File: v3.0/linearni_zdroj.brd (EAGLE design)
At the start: 39.4 x 77.1 mm, 37 parts, among them IC1 LM358N, IC2 LM358N, Q1 IRFZ34NAV, Q2 TIP120

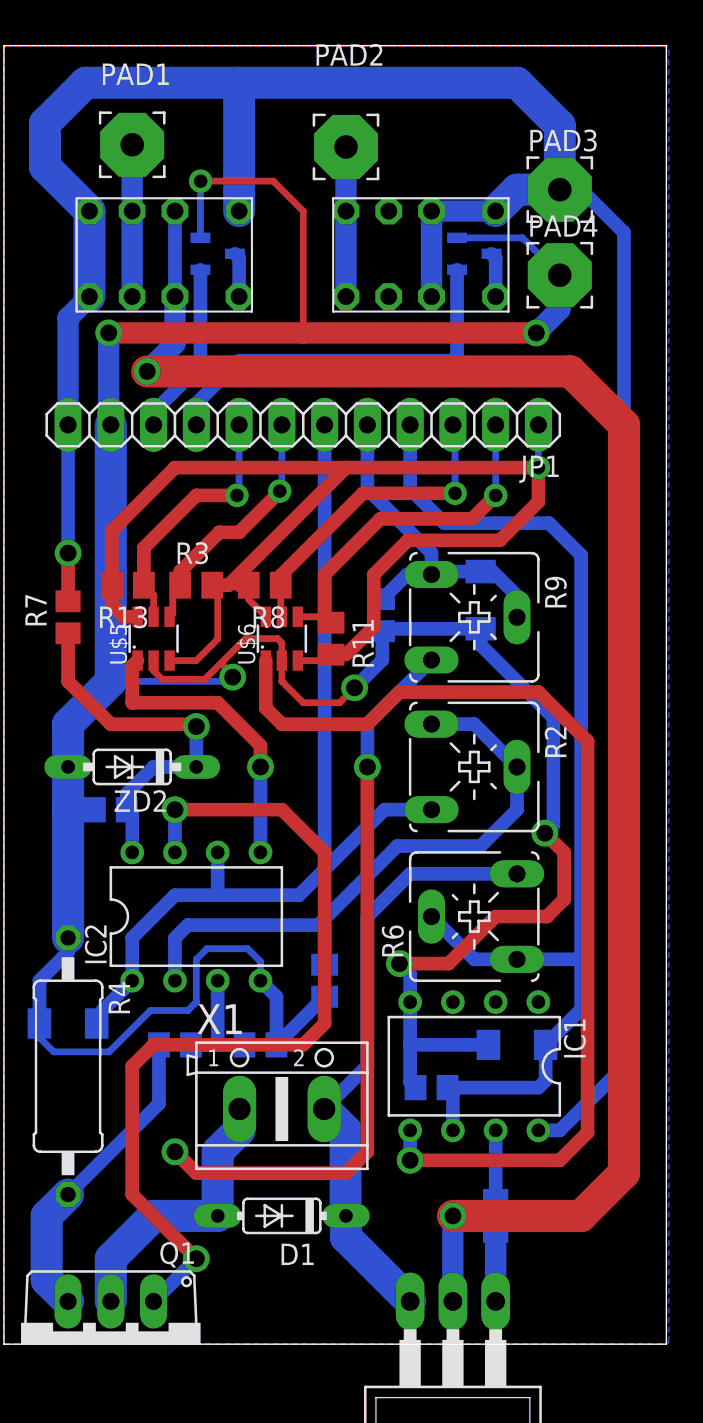
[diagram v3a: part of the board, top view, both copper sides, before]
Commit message: přidání 3D modelu úpravy dokumentace
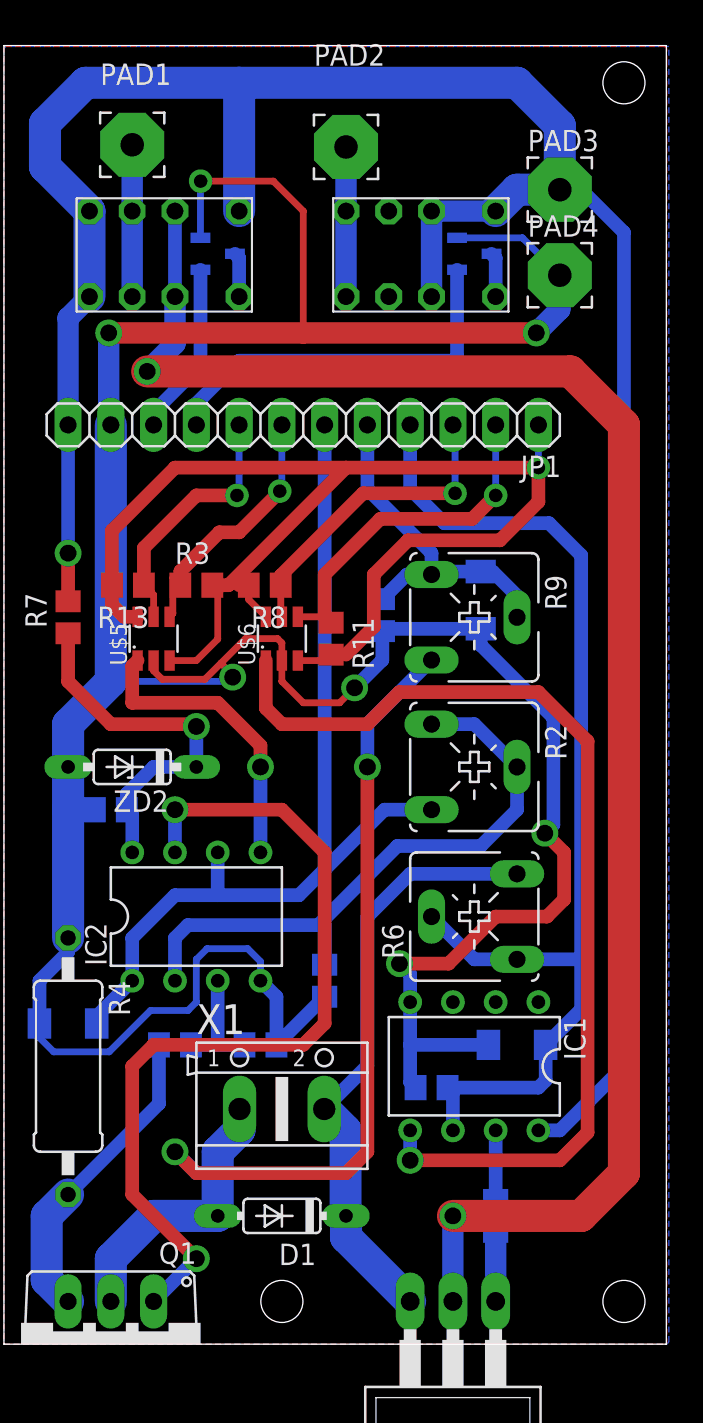
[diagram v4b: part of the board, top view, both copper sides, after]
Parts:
- R1, R11, R13, R3, R8: device rcl_my:M0805 -> rcl:R0805

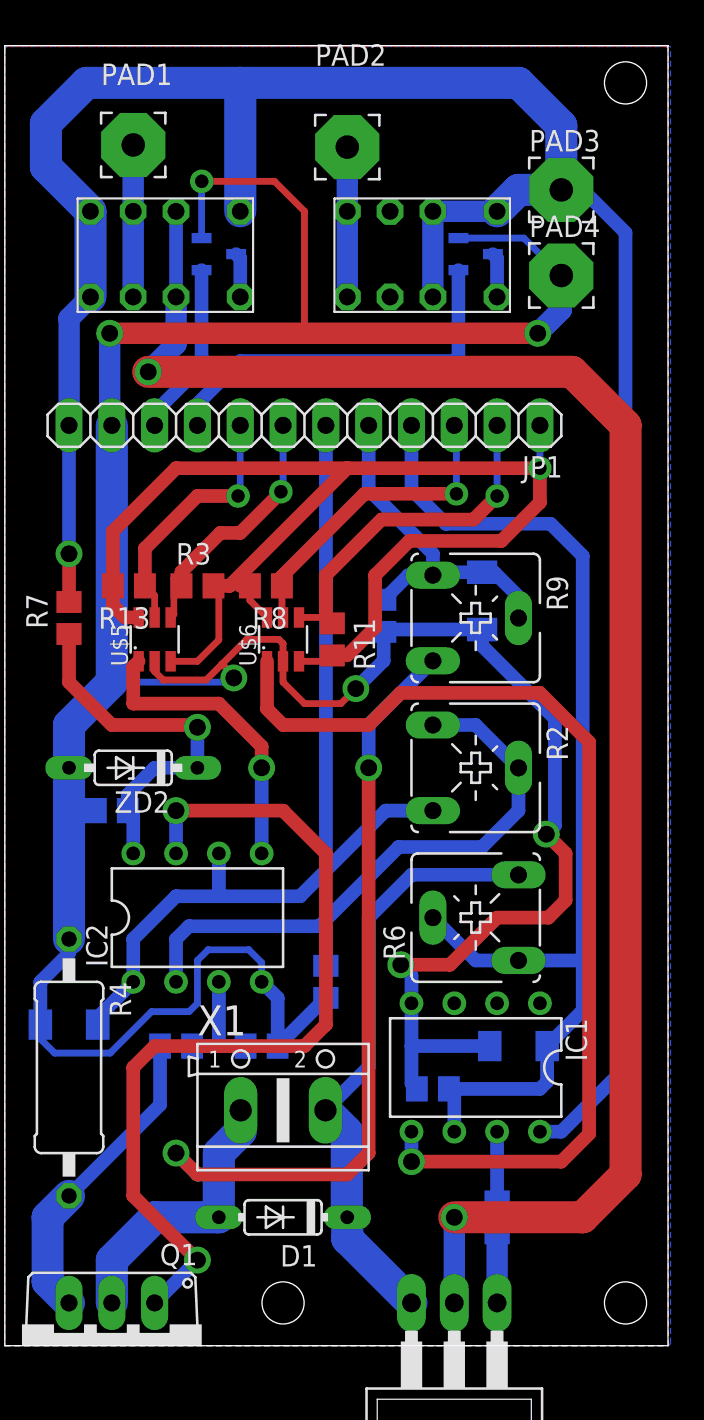
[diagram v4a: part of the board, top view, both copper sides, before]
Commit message: upratování schémy, dokumentace lineárního regulátoru napětí
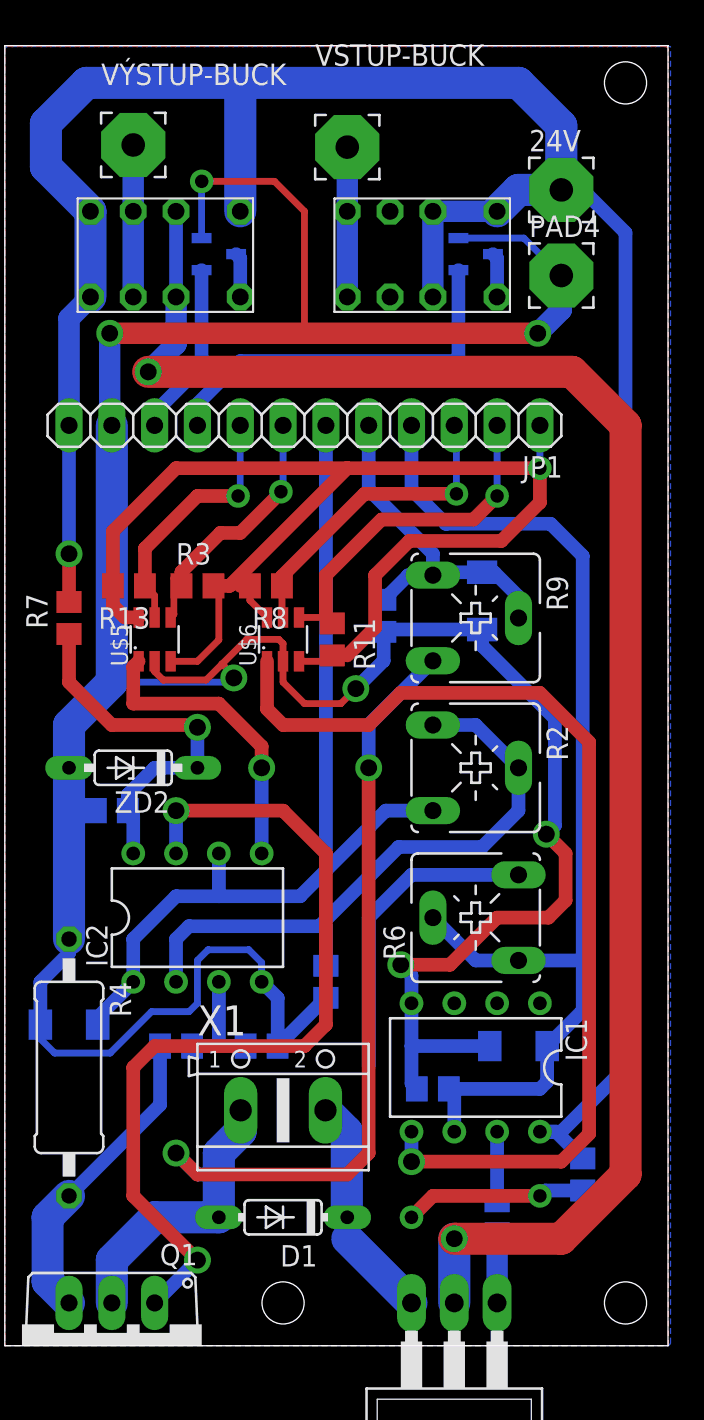
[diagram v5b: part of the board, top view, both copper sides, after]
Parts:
- added C2: 10n, rcl:C0805
- R11, R8: value (none) -> 5K
- R12: value (none) -> 360R
- renumbered PAD1 to VÝSTUP-BUCK, PAD2 to VSTUP-BUCK, PAD3 to 24V
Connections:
- net N$13 renamed +
- net N$8 renamed NAPAJENI-REG
- net +24V: now also C2.1
- net GND: now also C2.2
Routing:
- net GND: track 206.7 -> 217.5 mm, vias 7 -> 9
- net +: track 36.0 -> 31.1 mm
- net +24V: track 148.3 -> 151.5 mm
- net NAPAJENI-REG: track 100.6 -> 99.8 mm

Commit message: zase sem se jednou ve škole něco naučil
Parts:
- removed C1: (no value), rcl:C0805
- moved R14 13.1 mm to (16.5, 6.35), flipped to the top, turned to 180 degrees
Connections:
- removed net N$1: Q1.S, R14.2, R4.2
- net GND: now also R14.1; no longer C1.2
- net N$2: now also R14.2
- net N$20: now also Q1.S, R4.2; no longer C1.1, R14.1
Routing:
- net N$1: track 18.5 -> 0.00 mm
- net N$20: track 6.99 -> 23.8 mm
- net N$2: track 51.7 -> 56.4 mm
- net GND: track 217.5 -> 219.1 mm, vias 9 -> 11
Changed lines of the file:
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@@
 <attribute name="VALUE" x="8.636" y="47.625" size="1.27" layer="27" rot="R180"/>
-</element>
-<element name="R14" library="rcl" library_urn="urn:adsk.eagle:library:334" package="R0805" package3d_urn="urn:adsk.eagle:package:23553/2" value="" x="10.16" y="17.78" smashed="yes" rot="MR0">
-<attribute name="NAME" x="10.795" y="19.05" size="1.27" layer="26" rot="MR0"/>
-<attribute name="POPULARITY" value="86" x="10.16" y="17.78" size="1.778" layer="28" rot="MR0" display="off"/>
-<attribute name="SPICEPREFIX" value="R" x="10.16" y="17.78" size="1.778" layer="28" rot="MR0" display="off"/>
-<attribute name="VALUE" x="10.795" y="15.24" size="1.27" layer="28" rot="MR0"/>
-</element>
-<element name="C1" library="rcl" library_urn="urn:adsk.eagle:library:334" package="C0805" package3d_urn="urn:adsk.eagle:package:23617/2" value="" x="15.24" y="17.78" smashed="yes" rot="MR180">
-<attribute name="NAME" x="13.97" y="16.51" size="1.27" layer="26" rot="MR180"/>
-<attribute name="POPULARITY" value="88" x="15.24" y="17.78" size="1.778" layer="28" rot="MR180" display="off"/>
-<attribute name="SPICEPREFIX" value="C" x="15.24" y="17.78" size="1.778" layer="28" rot="MR180" display="off"/>
-<attribute name="VALUE" x="13.97" y="20.32" size="1.27" layer="28" rot="MR180"/>
 </element>
 <element name="Q1" library="devices" package="TO220AV" override_package3d_urn="urn:adsk.eagle:package:33936961/2" override_package_urn="urn:adsk.eagle:footprint:33936962/1" value="IRFZ34NAV" x="6.35" y="0" smashed="yes" rot="R180">
@@
 <attribute name="VALUE" x="36.83" y="11.43" size="1.27" layer="28" rot="MR270"/>
 </element>
+<element name="R14" library="rcl" library_urn="urn:adsk.eagle:library:334" package="R0805" package3d_urn="urn:adsk.eagle:package:23553/2" value="" x="16.51" y="6.35" smashed="yes" rot="R180">
+<attribute name="NAME" x="17.145" y="5.08" size="1.27" layer="25" rot="R180"/>
+<attribute name="POPULARITY" value="86" x="16.51" y="6.35" size="1.778" layer="27" rot="R180" display="off"/>
+<attribute name="SPICEPREFIX" value="R" x="16.51" y="6.35" size="1.778" layer="27" rot="R180" display="off"/>
+<attribute name="VALUE" x="17.145" y="8.89" size="1.27" layer="27" rot="R180"/>
+</element>
 </elements>
 <signals>
-<signal name="N$1">
-<contactref element="R4" pad="2"/>
-<contactref element="R14" pad="2"/>
-<contactref element="Q1" pad="S"/>
-<wire x1="3.81" y1="2.54" x2="2.54" y2="3.81" width="1.905" layer="16"/>
-<wire x1="2.54" y1="7.62" x2="3.81" y2="8.89" width="1.905" layer="16"/>
-<wire x1="2.54" y1="3.81" x2="2.54" y2="7.62" width="1.905" layer="16"/>
-<wire x1="9.21" y1="17.78" x2="9.21" y2="14.29" width="0.8128" layer="16"/>
-<wire x1="9.21" y1="14.29" x2="3.81" y2="8.89" width="0.8128" layer="16"/>
-</signal>
 <signal name="N$3">
 <contactref element="IC2" pad="2"/>
@@
 <contactref element="ZD3" pad="A"/>
 <contactref element="PAD4" pad="1"/>
-<contactref element="C1" pad="2"/>
 <wire x1="11.6753" y1="65.72" x2="11.6753" y2="69.0793" width="0.4064" layer="16"/>
 <wire x1="11.6753" y1="69.0793" x2="11.684" y2="69.088" width="0.4064" layer="16"/>
@@
 <wire x1="3.81" y1="23.29" x2="2.11" y2="21.59" width="0.8128" layer="16"/>
 <wire x1="3.81" y1="23.29" x2="3.81" y2="24.13" width="0.8128" layer="16"/>
-<wire x1="16.19" y1="17.78" x2="16.19" y2="20.64" width="0.8128" layer="16"/>
-<wire x1="16.19" y1="20.64" x2="15.24" y2="21.59" width="0.8128" layer="16"/>
-<wire x1="19.05" y1="20.64" x2="16.19" y2="17.78" width="0.8128" layer="16"/>
 <wire x1="6.35" y1="54.61" x2="6.35" y2="39.37" width="1.905" layer="16"/>
 <wire x1="3.81" y1="36.83" x2="3.81" y2="31.75" width="1.905" layer="16"/>
-<wire x1="3.81" y1="31.75" x2="3.81" y2="24.13" width="1.905" layer="16"/>
+<wire x1="3.81" y1="31.75" x2="3.81" y2="26.67" width="1.905" layer="16"/>
+<wire x1="3.81" y1="26.67" x2="3.81" y2="24.13" width="1.905" layer="16"/>
 <wire x1="6.35" y1="39.37" x2="3.81" y2="36.83" width="1.905" layer="16"/>
 <wire x1="16.51" y1="40.61" x2="16.51" y2="39.37" width="0.4064" layer="1"/>
@@
 <wire x1="13.589" y1="39.624" x2="13.335" y2="39.37" width="0.4064" layer="16"/>
 <wire x1="13.335" y1="39.37" x2="6.35" y2="39.37" width="0.4064" layer="16"/>
-<wire x1="10.9322" y1="19.8222" x2="8.7064125" y2="19.8222" width="0.4064" layer="16"/>
-<wire x1="8.7064125" y1="19.8222" x2="6.2500125" y2="17.3658" width="0.4064" layer="16"/>
-<wire x1="2.11" y1="18.21" x2="2.11" y2="19.05" width="0.4064" layer="16"/>
-<wire x1="11.43" y1="22.86" x2="11.43" y2="20.32" width="0.4064" layer="16"/>
-<wire x1="11.43" y1="20.32" x2="10.9322" y2="19.8222" width="0.4064" layer="16"/>
-<wire x1="6.2500125" y1="17.3658" x2="2.9542" y2="17.3658" width="0.4064" layer="16"/>
-<wire x1="2.9542" y1="17.3658" x2="2.11" y2="18.21" width="0.4064" layer="16"/>
-<wire x1="11.43" y1="22.86" x2="12.065" y2="23.495" width="0.4064" layer="16"/>
-<wire x1="12.065" y1="23.495" x2="14.478" y2="23.495" width="0.4064" layer="16"/>
-<wire x1="15.24" y1="22.733" x2="15.24" y2="21.59" width="0.4064" layer="16"/>
-<wire x1="15.24" y1="22.733" x2="14.478" y2="23.495" width="0.4064" layer="16"/>
 <wire x1="28.321" y1="42.496" x2="22.618" y2="42.496" width="0.8128" layer="16"/>
 <wire x1="22.618" y1="42.496" x2="22.479" y2="42.357" width="0.8128" layer="16"/>
@@
 <wire x1="24.13" y1="7.62" x2="25.4" y2="8.89" width="0.8128" layer="1"/>
 <wire x1="25.4" y1="8.89" x2="31.75" y2="8.89" width="0.8128" layer="1"/>
+<contactref element="R14" pad="1"/>
+<wire x1="17.46" y1="6.35" x2="18.73" y2="5.08" width="0.8128" layer="1"/>
+<wire x1="22.86" y1="5.08" x2="24.13" y2="6.35" width="0.8128" layer="1"/>
+<wire x1="24.13" y1="6.35" x2="24.13" y2="7.62" width="0.8128" layer="1"/>
+<wire x1="18.73" y1="5.08" x2="22.86" y2="5.08" width="0.8128" layer="1"/>
+<wire x1="16.51" y1="20.64" x2="19.05" y2="20.64" width="0.8128" layer="16"/>
+<wire x1="15.24" y1="21.59" x2="16.19" y2="20.64" width="0.8128" layer="16"/>
+<wire x1="16.19" y1="20.64" x2="16.51" y2="20.64" width="0.8128" layer="16"/>
+<via x="16.51" y="20.64" extent="1-16" drill="0.8"/>
+<wire x1="16.51" y1="20.64" x2="16.51" y2="22.86" width="0.8128" layer="1"/>
+<wire x1="7.62" y1="25.4" x2="6.35" y2="26.67" width="0.8128" layer="1"/>
+<via x="6.35" y="26.67" extent="1-16" drill="0.8"/>
+<wire x1="6.35" y1="26.67" x2="3.81" y2="26.67" width="0.8128" layer="16"/>
+<wire x1="16.51" y1="22.86" x2="13.97" y2="25.4" width="0.8128" layer="1"/>
+<wire x1="13.97" y1="25.4" x2="7.62" y2="25.4" width="0.8128" layer="1"/>
 </signal>
 <signal name="+">
@@
 <signal name="N$20">
 <contactref element="IC2" pad="3"/>
-<contactref element="R14" pad="1"/>
-<contactref element="C1" pad="1"/>
-<wire x1="14.29" y1="17.78" x2="12.7" y2="17.78" width="0.8128" layer="16"/>
-<wire x1="12.7" y1="17.78" x2="11.11" y2="17.78" width="0.8128" layer="16"/>
-<wire x1="12.7" y1="21.59" x2="12.7" y2="17.78" width="0.8128" layer="16"/>
+<wire x1="12.7" y1="17.78" x2="12.7" y2="21.59" width="0.8128" layer="16"/>
+<contactref element="R4" pad="2"/>
+<contactref element="Q1" pad="S"/>
+<wire x1="3.81" y1="2.54" x2="2.54" y2="3.81" width="1.905" layer="16"/>
+<wire x1="2.54" y1="7.62" x2="3.81" y2="8.89" width="1.905" layer="16"/>
+<wire x1="2.54" y1="3.81" x2="2.54" y2="7.62" width="1.905" layer="16"/>
+<wire x1="9.21" y1="14.29" x2="8.89" y2="13.97" width="0.8128" layer="16"/>
+<wire x1="8.89" y1="13.97" x2="3.81" y2="8.89" width="0.8128" layer="16"/>
+<wire x1="9.21" y1="14.29" x2="12.7" y2="17.78" width="0.8128" layer="16"/>
 </signal>
 <signal name="N$2">
@@
 <wire x1="7.62" y1="16.51" x2="7.62" y2="8.89" width="0.8128" layer="1"/>
 <wire x1="7.62" y1="8.89" x2="11.43" y2="5.08" width="0.8128" layer="1"/>
+<contactref element="R14" pad="2"/>
+<wire x1="11.43" y1="5.08" x2="14.29" y2="5.08" width="0.8128" layer="1"/>
+<wire x1="14.29" y1="5.08" x2="15.56" y2="6.35" width="0.8128" layer="1"/>
 </signal>
 <signal name="N$5">

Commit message: neumím malovat XD
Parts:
- removed ZD2: (no value), devices:DO35Z7
- Q2: value TIP120 -> (none); device transistor-power:TO220AH -> transistor:TO220V
- moved R7 32.0 mm to (7.62, 11.4)
- moved VSTUP-BUCK 16.9 mm to (3.81, 67.3)
- moved U$4 15.3 mm to (22.9, 76.2)
- moved U$2 12.5 mm to (15.2, 76.2)
- moved VÝSTUP-BUCK 10.9 mm to (3.81, 81.4)
- moved U$1 10.2 mm to (15.2, 66.0)
- moved Q2 3.81 mm to (26.7, 0.00)
- moved U$3 2.84 mm to (26.7, 67.3), turned to 270 degrees
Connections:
- removed net N$5: C9.1, IC2.8, R7.1, ZD2.C
- new net N$1: IC2.7, R7.2
- net +: now also Q2.3; no longer Q2.E
- net +24V: now also C9.1, IC2.8; no longer R7.2
- net GND: no longer ZD2.A
- net N$2: now also R7.1; no longer IC2.7
- net N$4: now also Q2.1; no longer Q2.B
- net NAPAJENI-REG: now also Q2.2; no longer Q2.C
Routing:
- net N$2: track 56.4 -> 16.5 mm, vias 2 -> 1
- net N$1: track 0.00 -> 37.2 mm, vias 0 -> 1
- net N$5: track 22.4 -> 0.00 mm, vias 1 -> 0
- net +24V: track 151.5 -> 173.2 mm, vias 1 -> 2
- net PA8: track 10.4 -> 30.3 mm, vias 0 -> 2
- net GND: track 219.1 -> 234.5 mm
- net NAPAJENI-REG: track 99.8 -> 114.5 mm
- net N$10: track 9.02 -> 19.8 mm
- net +: track 31.1 -> 36.0 mm
- net N$19: track 8.89 -> 12.7 mm
- net N$17: track 2.64 -> 3.84 mm
- net N$6: track 17.7 -> 16.7 mm
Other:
- board size 39.4 x 77.1 mm -> 39.4 x 87.3 mm

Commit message: pokračování v doku úklid schéma
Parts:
- C9: value (none) -> 10n
- D1: value (none) -> 1N4001
- ER1, ER2: value V23105-A5305-A201 -> V23105-A5305
- Q2: value (none) -> TIP120
- Q3, Q4: value NX3008 -> 2N7002
- R1, R10: value (none) -> 1K
- R13, R3: value (none) -> 5K
- R14: value (none) -> 100K
- R2: value (none) -> 10K(9K)
- R7: value (none) -> 20K
- R9: value (none) -> 10K(7K)
- ZD1, ZD3, ZD4: value (none) -> 3,3V
- renumbered PAD4 to GND, R4 to RS, U$1 to ER1, U$2 to ER2, U$3 to Q3, U$4 to Q4, X1 to -
